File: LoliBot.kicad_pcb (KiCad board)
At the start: 2 copper layers, 146 x 100 mm, 32 parts, among them J1 LOLINBATT, J10 LEFT-MOTOR, J11 REFLECT_, J12 MECH, J13 MECH, J14 MECH, J15 MECH, J16 MECH, J17 MECH, J18 MECH, J19 MECH, J2 APA106, J20 CONN_01X08, J21 CONN_01X06, J22 BRIDGE, J23 BRIDGE, J3 SERVO1, J4 RIGHT, J5 LEFT, J6 MPU-9250, J7 APA106, J8 APA106, J9 RIGHT-MOTOR, SW1 SPST, U1 LOLIN32-LITE, U3 L9110, U4 L9110

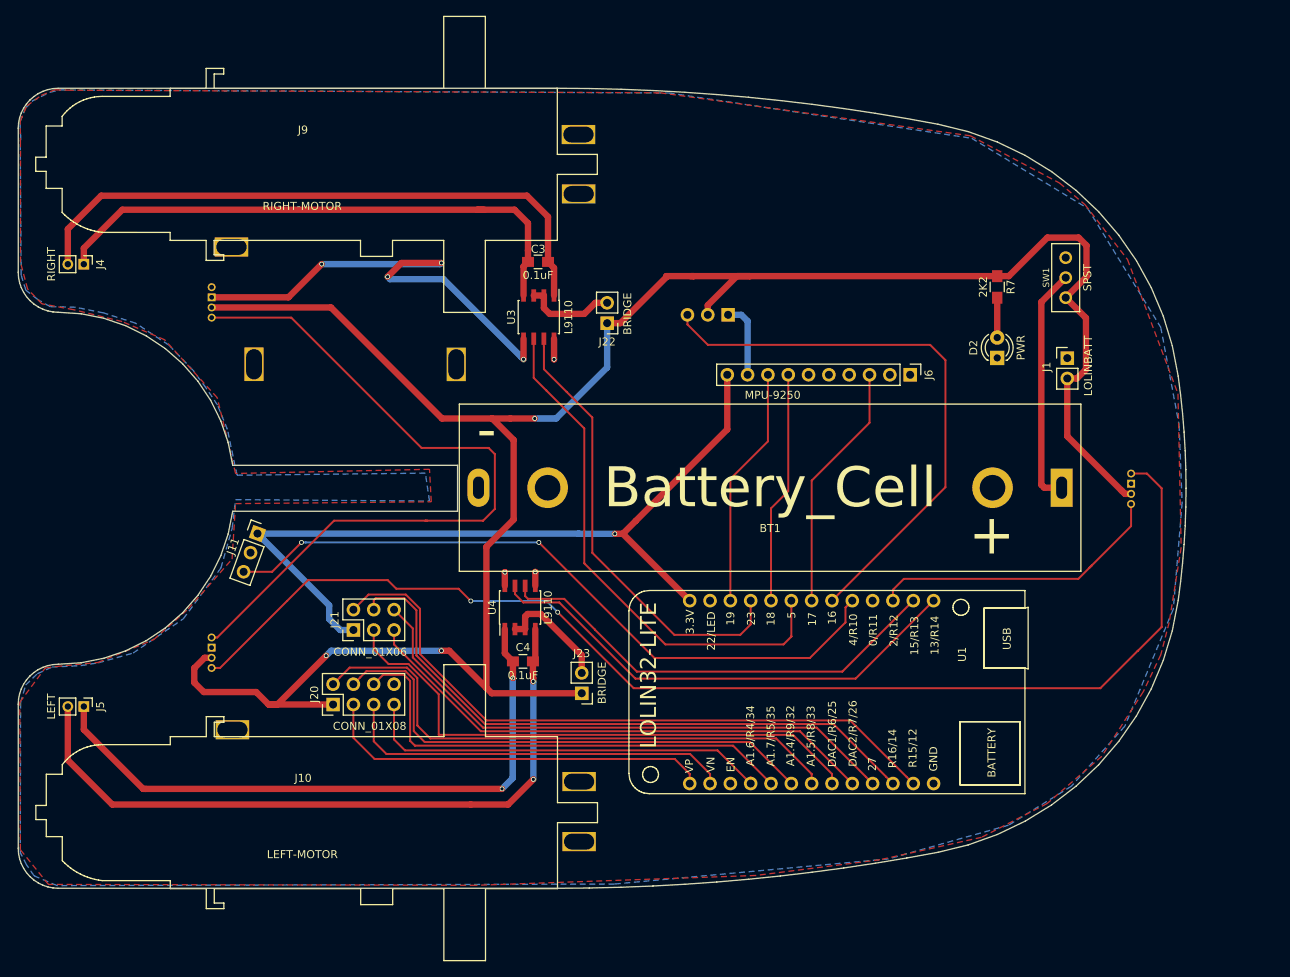
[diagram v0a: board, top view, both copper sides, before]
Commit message: Added Fuse.  Updated pcb
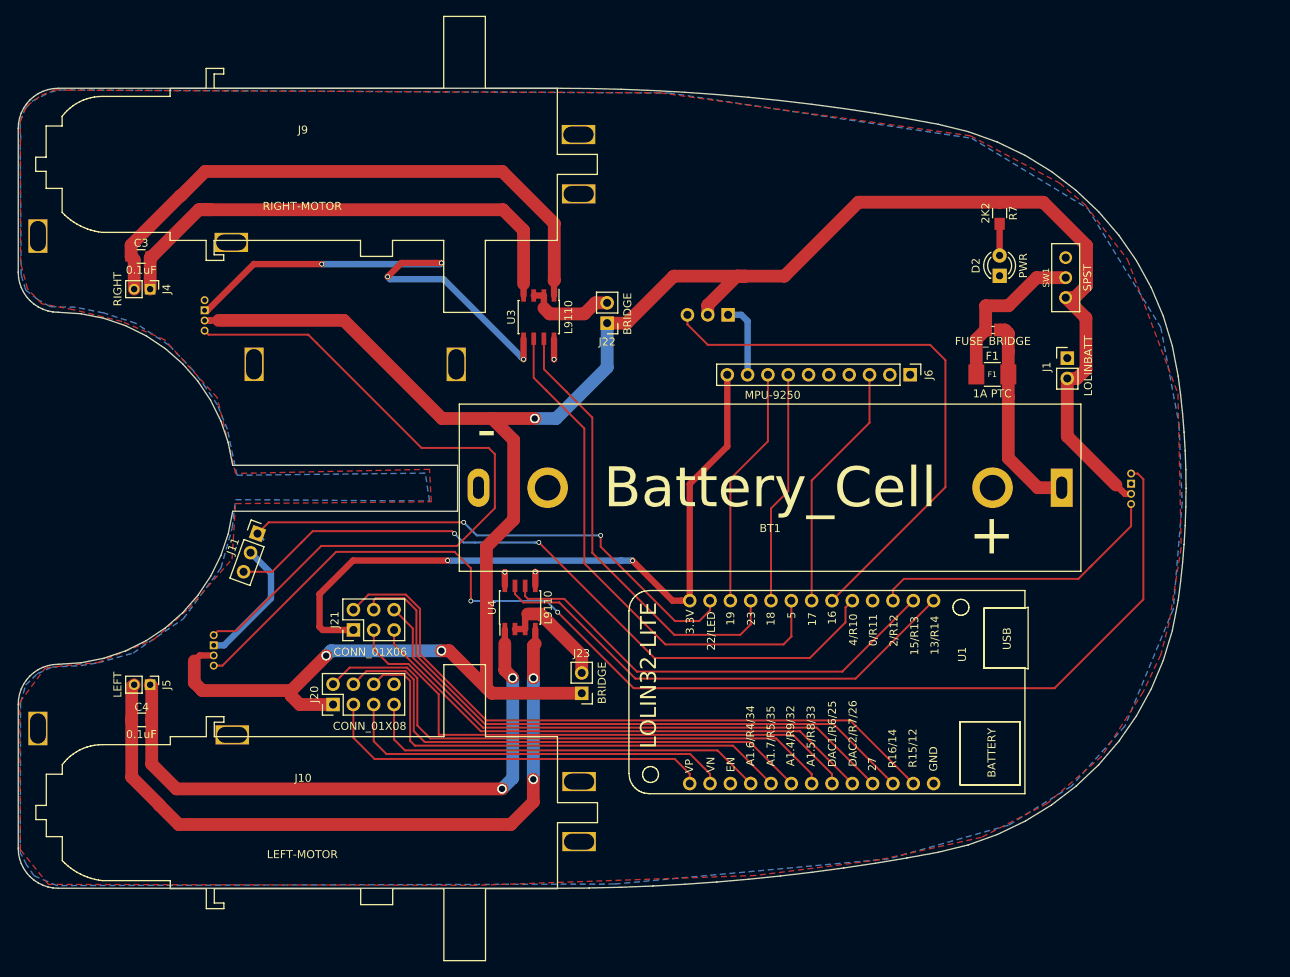
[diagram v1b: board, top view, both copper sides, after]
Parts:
- added F1: 1A PTC, Resistors_SMD:R_1210_HandSoldering, F.Cu at (172.7, 75.0)
- added J24: FUSE_BRIDGE, libs:bridge, F.Cu at (172.8, 69.5)
- added J25: MECH, Mounting_Holes:MountingHole_3.2mm_M3_Pad, F.Cu at (53.4, 119.3)
- added J26: MECH, Mounting_Holes:MountingHole_3.2mm_M3_Pad, F.Cu at (53.4, 57.7)
- moved C3 49.6 mm to (66.3, 60.3), turned to 0 degrees
- moved C4 48.2 mm to (66.4, 118.2), turned to 180 degrees
- moved D2 10.3 mm to (173.7, 62.7)
- moved R7 9.25 mm to (173.7, 54.9)
- moved J4 8.86 mm to (67.5, 64.4)
- moved J5 8.73 mm to (67.5, 113.8)
- moved J8 1.85 mm to (74.3, 67.7)
- moved J16 0.65 mm to (77.7, 120.1)
- moved J17 0.57 mm to (77.6, 58.5)
- moved J7 0.39 mm to (75.4, 109.5)
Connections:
- J11 pad 1: +3V3 -> /IO22
- SW1 pad 2: Net-(BT1-Pad1) -> Net-(F1-Pad1)
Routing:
- net /IO22: track 0.00 -> 65.9 mm, vias 0 -> 2
- net Net-(F1-Pad1): track 0.00 -> 20.5 mm
- net GND: track 77.3 -> 95.2 mm
- net /BATT_V: track 278.5 -> 291.3 mm
- net +3V3: track 100.8 -> 88.8 mm, vias 1 -> 2
- net Net-(C3-Pad2): track 70.3 -> 63.2 mm
- net Net-(BT1-Pad1): track 29.6 -> 25.0 mm
- net Net-(C3-Pad1): track 77.4 -> 74.1 mm
- net Net-(C4-Pad1): track 79.2 -> 76.0 mm
- net /IO4: track 87.7 -> 88.8 mm
- net Net-(D2-Pad2): track 4.98 -> 3.96 mm
- net Net-(J2-Pad4): track 154.0 -> 153.0 mm

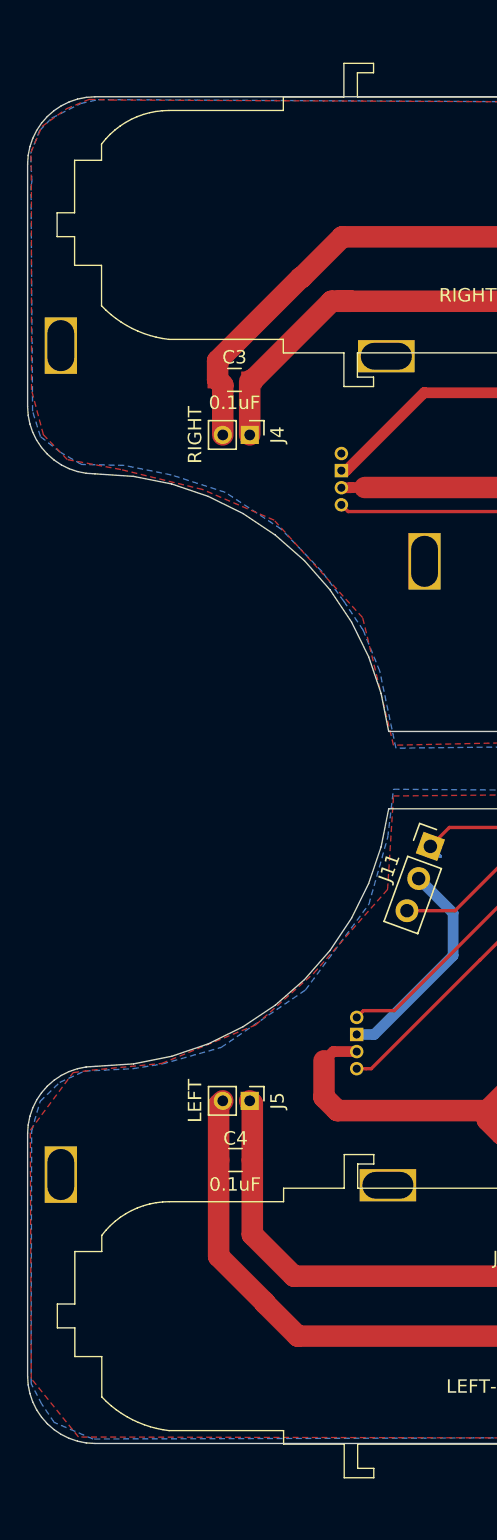
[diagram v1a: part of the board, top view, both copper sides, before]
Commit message: Added Through holes for cable ties
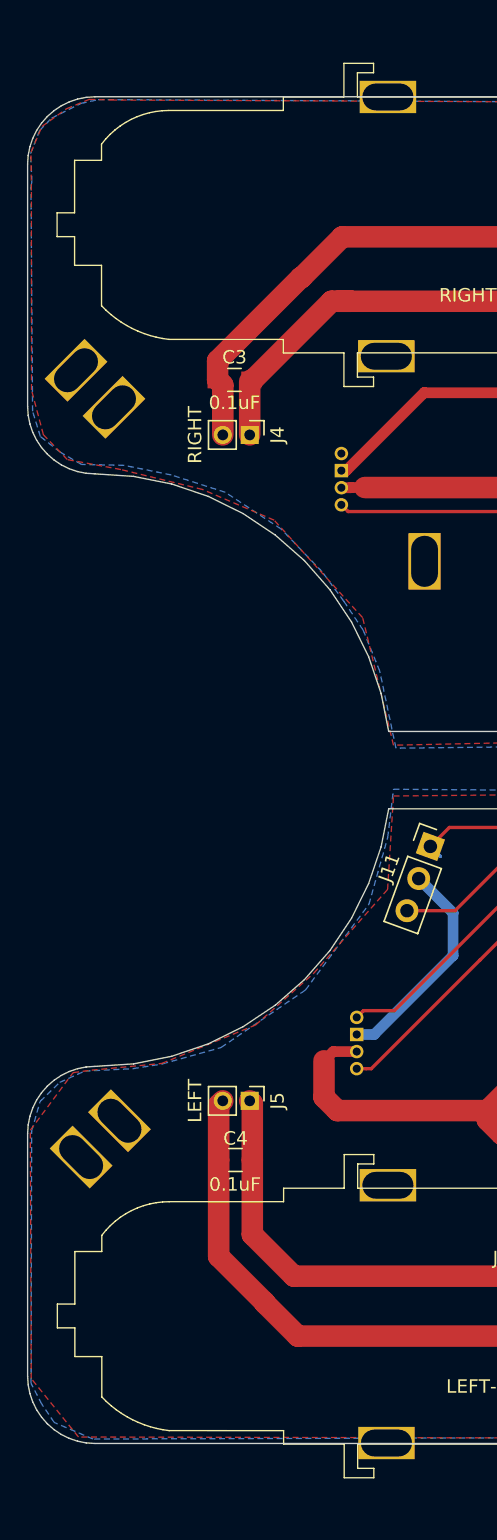
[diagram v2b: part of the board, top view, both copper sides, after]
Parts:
- added J27: MECH, Mounting_Holes:MountingHole_3.2mm_M3_Pad, F.Cu at (57.8, 115.3)
- added J28: MECH, Mounting_Holes:MountingHole_3.2mm_M3_Pad, F.Cu at (57.4, 62.3)
- added J29: MECH, Mounting_Holes:MountingHole_3.2mm_M3_Pad, F.Cu at (77.7, 39.3)
- added J30: MECH, Mounting_Holes:MountingHole_3.2mm_M3_Pad, F.Cu at (77.6, 139.2)
- moved J26 2.15 mm to (54.6, 59.6), turned to 45 degrees
- moved J25 1.99 mm to (55.0, 118.0), turned to 315 degrees
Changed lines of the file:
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@@
     (tracks 380)
     (zones 0)
-    (modules 36)
-    (nets 55)
+    (modules 40)
+    (nets 59)
   )
   (page A4)
@@
   (net 53 "Net-(J25-Pad1)")
   (net 54 "Net-(J26-Pad1)")
+  (net 55 "Net-(J27-Pad1)")
+  (net 56 "Net-(J28-Pad1)")
+  (net 57 "Net-(J29-Pad1)")
+  (net 58 "Net-(J30-Pad1)")
   (net_class Default "This is the default net class."
     (clearance 0.2)
@@
     (add_net "Net-(J25-Pad1)")
     (add_net "Net-(J26-Pad1)")
+    (add_net "Net-(J27-Pad1)")
+    (add_net "Net-(J28-Pad1)")
+    (add_net "Net-(J29-Pad1)")
+    (add_net "Net-(J30-Pad1)")
     (add_net "Net-(J7-Pad4)")
     (add_net "Net-(J8-Pad4)")
@@
   )
   (module Mounting_Holes:MountingHole_3.2mm_M3_Pad (layer F.Cu)
-    (at 53.44668 119.28856 90)
+    (at 54.95544 117.99316 315)
     (descr "Mounting Hole 3.2mm, M3")
     (tags "mounting hole 3.2mm m3")
     (attr virtual)
-    (fp_text reference J25 (at 0 -4.2 90) (layer F.SilkS) hide
-      (effects (font (size 1 1) (thickness 0.15)))
-    )
-    (fp_text value MECH (at 0 4.2 90) (layer F.Fab) hide
-      (effects (font (size 1 1) (thickness 0.15)))
-    )
-    (fp_text user %R (at 0.3 0 90) (layer F.Fab)
+    (fp_text reference J25 (at 0 -4.2 315) (layer F.SilkS) hide
+      (effects (font (size 1 1) (thickness 0.15)))
+    )
+    (fp_text value MECH (at 0 4.2 315) (layer F.Fab) hide
+      (effects (font (size 1 1) (thickness 0.15)))
+    )
+    (fp_text user %R (at 0.3 0 315) (layer F.Fab)
       (effects (font (size 1 1) (thickness 0.15)))
     )
     (fp_circle (center 0 0) (end 3.2 0) (layer Cmts.User) (width 0.15))
     (fp_circle (center 0 0) (end 3.45 0) (layer F.CrtYd) (width 0.05))
-    (pad 1 thru_hole rect (at 0 0 90) (size 4.2 2.4) (drill oval 3.8 2) (layers *.Cu *.Mask)
+    (pad 1 thru_hole rect (at 0 0 315) (size 4.2 2.4) (drill oval 3.8 2) (layers *.Cu *.Mask)
       (net 53 "Net-(J25-Pad1)"))
   )
   (module Mounting_Holes:MountingHole_3.2mm_M3_Pad (layer F.Cu)
-    (at 53.44668 57.73928 90)
+    (at 54.57444 59.56808 45)
     (descr "Mounting Hole 3.2mm, M3")
     (tags "mounting hole 3.2mm m3")
     (attr virtual)
-    (fp_text reference J26 (at 0 -4.2 90) (layer F.SilkS) hide
-      (effects (font (size 1 1) (thickness 0.15)))
-    )
-    (fp_text value MECH (at 0 4.2 90) (layer F.Fab) hide
-      (effects (font (size 1 1) (thickness 0.15)))
-    )
-    (fp_text user %R (at 0.3 0 90) (layer F.Fab)
+    (fp_text reference J26 (at 0 -4.2 45) (layer F.SilkS) hide
+      (effects (font (size 1 1) (thickness 0.15)))
+    )
+    (fp_text value MECH (at 0 4.2 45) (layer F.Fab) hide
+      (effects (font (size 1 1) (thickness 0.15)))
+    )
+    (fp_text user %R (at 0.3 0 45) (layer F.Fab)
       (effects (font (size 1 1) (thickness 0.15)))
     )
     (fp_circle (center 0 0) (end 3.2 0) (layer Cmts.User) (width 0.15))
     (fp_circle (center 0 0) (end 3.45 0) (layer F.CrtYd) (width 0.05))
-    (pad 1 thru_hole rect (at 0 0 90) (size 4.2 2.4) (drill oval 3.8 2) (layers *.Cu *.Mask)
+    (pad 1 thru_hole rect (at 0 0 45) (size 4.2 2.4) (drill oval 3.8 2) (layers *.Cu *.Mask)
       (net 54 "Net-(J26-Pad1)"))
   )
@@
     )
   )
+  (module Mounting_Holes:MountingHole_3.2mm_M3_Pad (layer F.Cu)
+    (at 57.80024 115.29568 315)
+    (descr "Mounting Hole 3.2mm, M3")
+    (tags "mounting hole 3.2mm m3")
+    (attr virtual)
+    (fp_text reference J27 (at 0 -4.2 315) (layer F.SilkS) hide
+      (effects (font (size 1 1) (thickness 0.15)))
+    )
+    (fp_text value MECH (at 0 4.2 315) (layer F.Fab) hide
+      (effects (font (size 1 1) (thickness 0.15)))
+    )
+    (fp_text user %R (at 0.3 0 315) (layer F.Fab)
+      (effects (font (size 1 1) (thickness 0.15)))
+    )
+    (fp_circle (center 0 0) (end 3.2 0) (layer Cmts.User) (width 0.15))
+    (fp_circle (center 0 0) (end 3.45 0) (layer F.CrtYd) (width 0.05))
+    (pad 1 thru_hole rect (at 0 0 315) (size 4.2 2.4) (drill oval 3.8 2) (layers *.Cu *.Mask)
+      (net 55 "Net-(J27-Pad1)"))
+  )
+  (module Mounting_Holes:MountingHole_3.2mm_M3_Pad (layer F.Cu)
+    (at 57.39384 62.32144 45)
+    (descr "Mounting Hole 3.2mm, M3")
+    (tags "mounting hole 3.2mm m3")
+    (attr virtual)
+    (fp_text reference J28 (at 0 -4.2 45) (layer F.SilkS) hide
+      (effects (font (size 1 1) (thickness 0.15)))
+    )
+    (fp_text value MECH (at 0 4.2 45) (layer F.Fab) hide
+      (effects (font (size 1 1) (thickness 0.15)))
+    )
+    (fp_text user %R (at 0.3 0 45) (layer F.Fab)
+      (effects (font (size 1 1) (thickness 0.15)))
+    )
+    (fp_circle (center 0 0) (end 3.2 0) (layer Cmts.User) (width 0.15))
+    (fp_circle (center 0 0) (end 3.45 0) (layer F.CrtYd) (width 0.05))
+    (pad 1 thru_hole rect (at 0 0 45) (size 4.2 2.4) (drill oval 3.8 2) (layers *.Cu *.Mask)
+      (net 56 "Net-(J28-Pad1)"))
+  )
+  (module Mounting_Holes:MountingHole_3.2mm_M3_Pad (layer F.Cu)
+    (at 77.73416 39.27348)
+    (descr "Mounting Hole 3.2mm, M3")
+    (tags "mounting hole 3.2mm m3")
+    (attr virtual)
+    (fp_text reference J29 (at 0 -4.2) (layer F.SilkS) hide
+      (effects (font (size 1 1) (thickness 0.15)))
+    )
+    (fp_text value MECH (at 0 4.2) (layer F.Fab) hide
+      (effects (font (size 1 1) (thickness 0.15)))
+    )
+    (fp_text user %R (at 0.3 0) (layer F.Fab)
+      (effects (font (size 1 1) (thickness 0.15)))
+    )
+    (fp_circle (center 0 0) (end 3.2 0) (layer Cmts.User) (width 0.15))
+    (fp_circle (center 0 0) (end 3.45 0) (layer F.CrtYd) (width 0.05))
+    (pad 1 thru_hole rect (at 0 0) (size 4.2 2.4) (drill oval 3.8 2) (layers *.Cu *.Mask)
+      (net 57 "Net-(J29-Pad1)"))
+  )
+  (module Mounting_Holes:MountingHole_3.2mm_M3_Pad (layer F.Cu)
+    (at 77.62748 139.22756)
+    (descr "Mounting Hole 3.2mm, M3")
+    (tags "mounting hole 3.2mm m3")
+    (attr virtual)
+    (fp_text reference J30 (at 0 -4.2) (layer F.SilkS) hide
+      (effects (font (size 1 1) (thickness 0.15)))
+    )
+    (fp_text value MECH (at 0 4.2) (layer F.Fab) hide
+      (effects (font (size 1 1) (thickness 0.15)))
+    )
+    (fp_text user %R (at 0.3 0) (layer F.Fab)
+      (effects (font (size 1 1) (thickness 0.15)))
+    )
+    (fp_circle (center 0 0) (end 3.2 0) (layer Cmts.User) (width 0.15))
+    (fp_circle (center 0 0) (end 3.45 0) (layer F.CrtYd) (width 0.05))
+    (pad 1 thru_hole rect (at 0 0) (size 4.2 2.4) (drill oval 3.8 2) (layers *.Cu *.Mask)
+      (net 58 "Net-(J30-Pad1)"))
+  )
   (gr_line (start 109.331348 76.073309) (end 109.331348 78.573309) (layer B.SilkS) (width 0.1))

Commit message: Started silkscreen
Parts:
- added G***: LOGO, libs:LCA2018_LOGO, F.Cu at (204.0, 38.1)
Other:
- board text added: "+"
- board text added: "-"
- board text added: "3.3V"
- board text added: "BAT_V"
- board text added: "GND"
- board text added: "IO12"
- board text added: "IO13"
- board text added: "IO14"
- board text added: "IO15"
- board text added: "IO16"
- board text added: "IO2"
- board text added: "IO23"
- board text added: "IO25"
- board text added: "IO26"
- board text added: "IO27"
- board text added: "IO32"
- board text added: "IO33"
- board text added: "IO34"
- board text added: "IO35"
- board text added: "IO5"
- board text added: "SERVO"
- board text added: "VN"
- board text added: "VP"
